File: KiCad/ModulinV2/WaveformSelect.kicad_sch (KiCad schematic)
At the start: 54 parts, among them IC10 TMUX4052DYYR, IC11 SN74AHCT1G00DBVR, IC12 SN74AHC1G02DBVR, IC13 TMUX4051DYYRQ1, IC14 TMUX4051DYYRQ1, IC15 SN74HC193DR, IC23 NC7SZ74K8X, IC24 SN74AHCT1G00DBVR, IC25 SN74AHC1G02DBVR, IC9 SN74AHCT1G00DBVR, J2 TSW-104-07-T-D, J6 TSW-104-07-T-D, J7 TSW-104-07-T-D, J8 TSW-104-07-T-D, U1 SN74AHC1G08DBVR

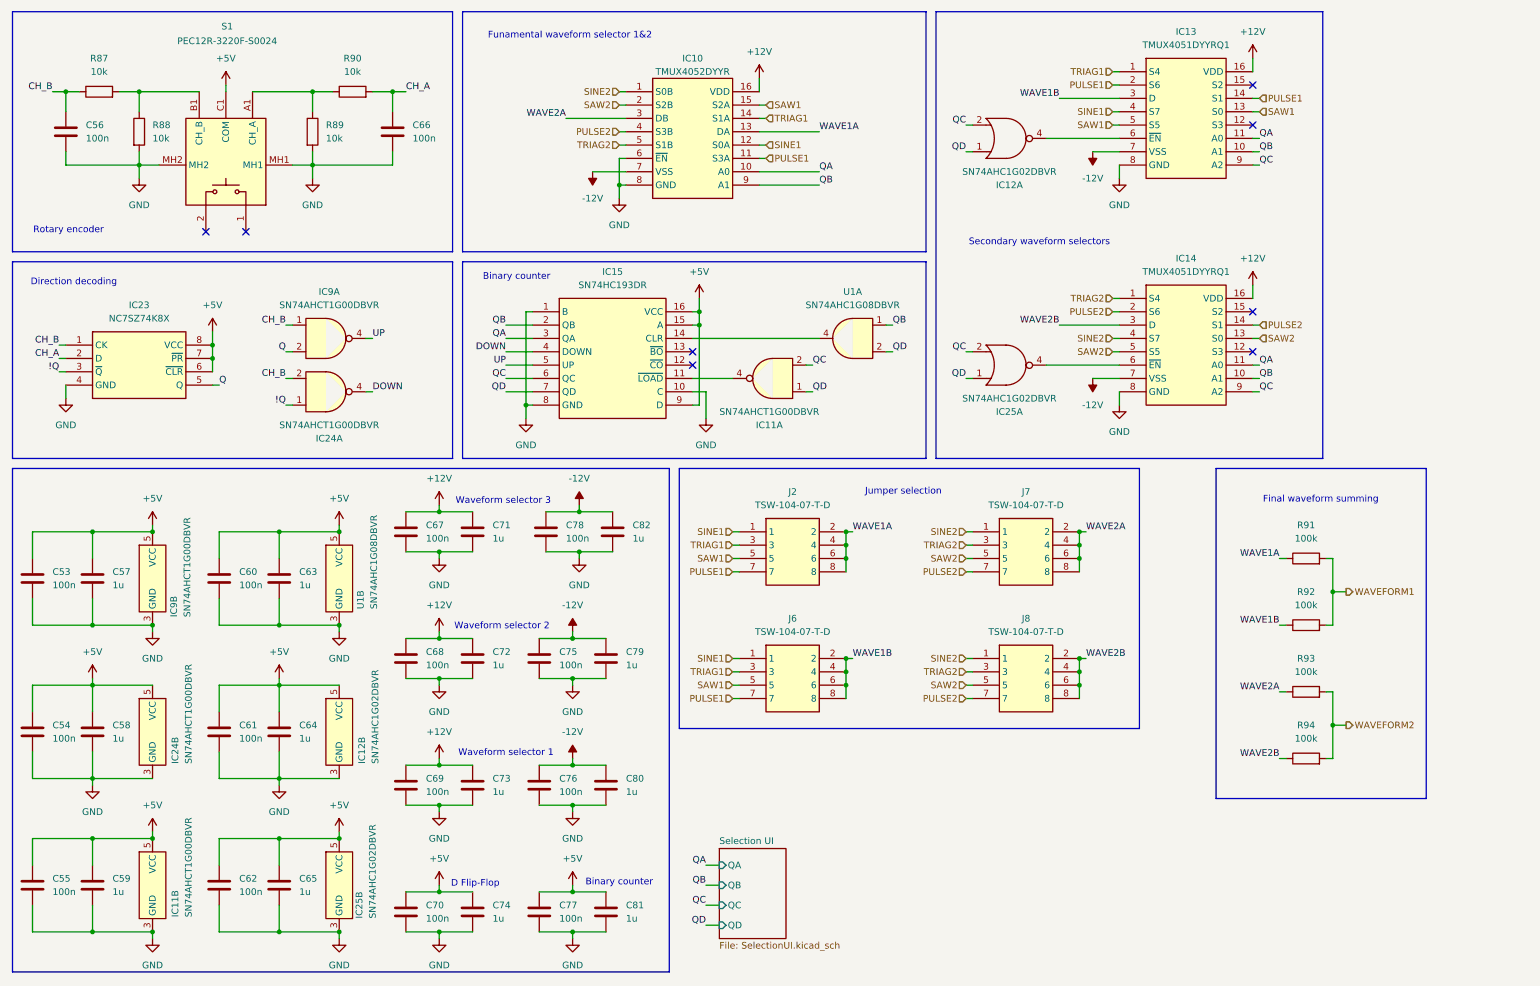
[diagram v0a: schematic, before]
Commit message: Changed switch for the boot and nrst. Fixed the GATE interface trigger
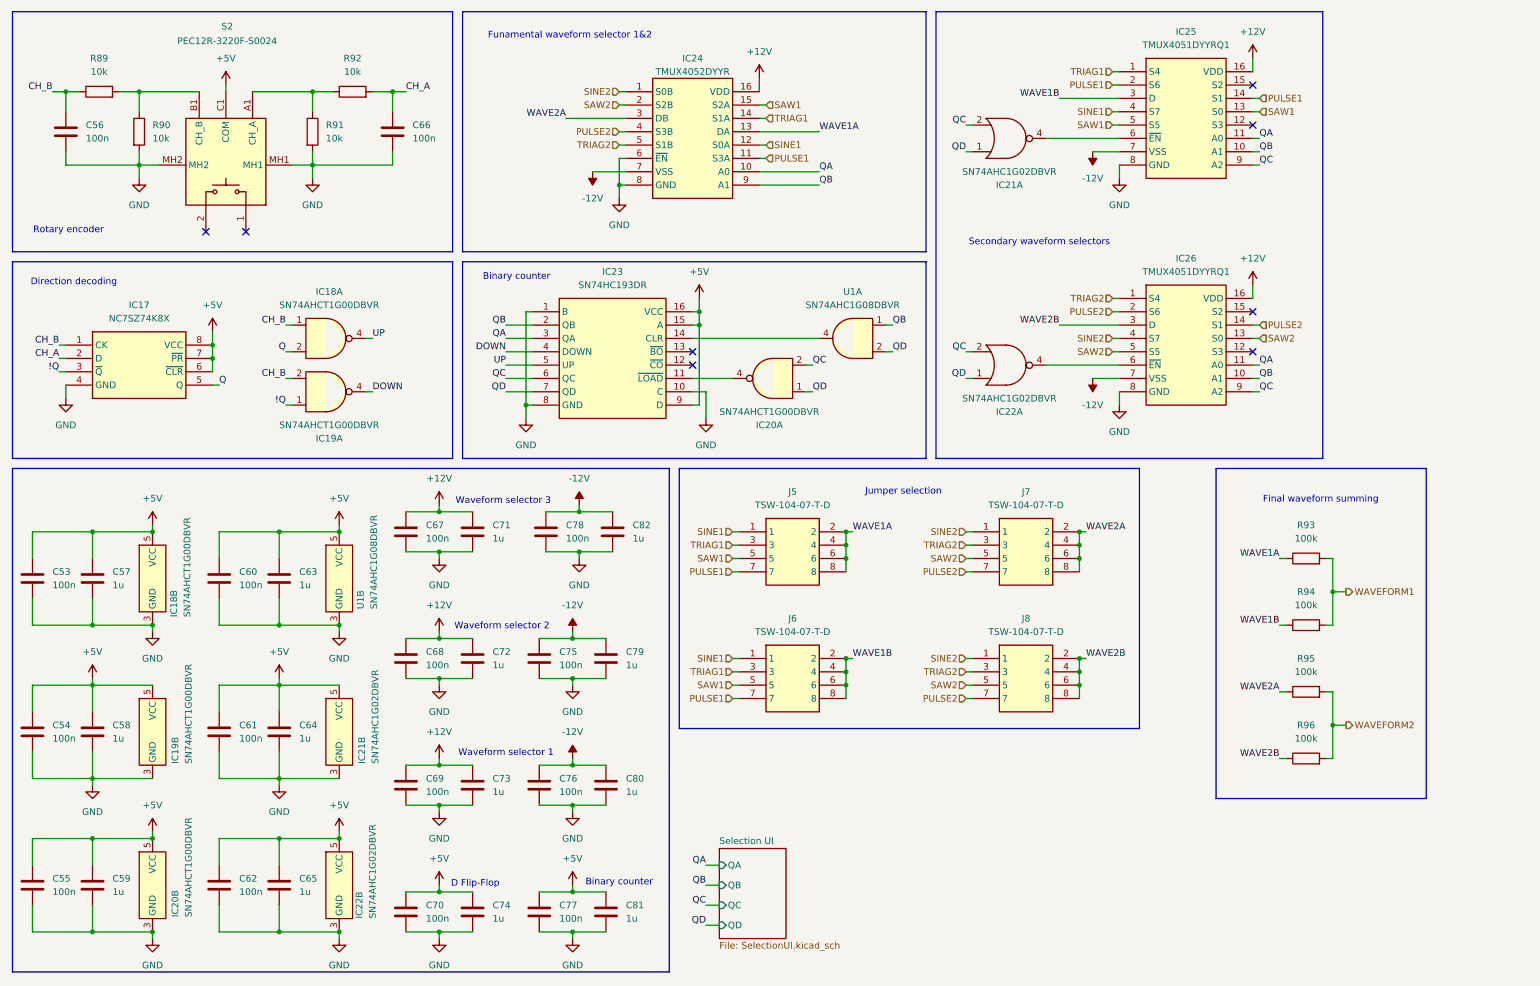
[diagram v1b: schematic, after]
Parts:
- renumbered IC23 to IC17, IC9 to IC18, IC24 to IC19, IC11 to IC20, IC12 to IC21, IC25 to IC22, IC15 to IC23, IC10 to IC24, IC13 to IC25, IC14 to IC26, J2 to J5, R87 to R89, R88 to R90, R89 to R91, R90 to R92, R91 to R93, R92 to R94, R93 to R95, R94 to R96, S1 to S2

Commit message: Started adding footprints for capacitors
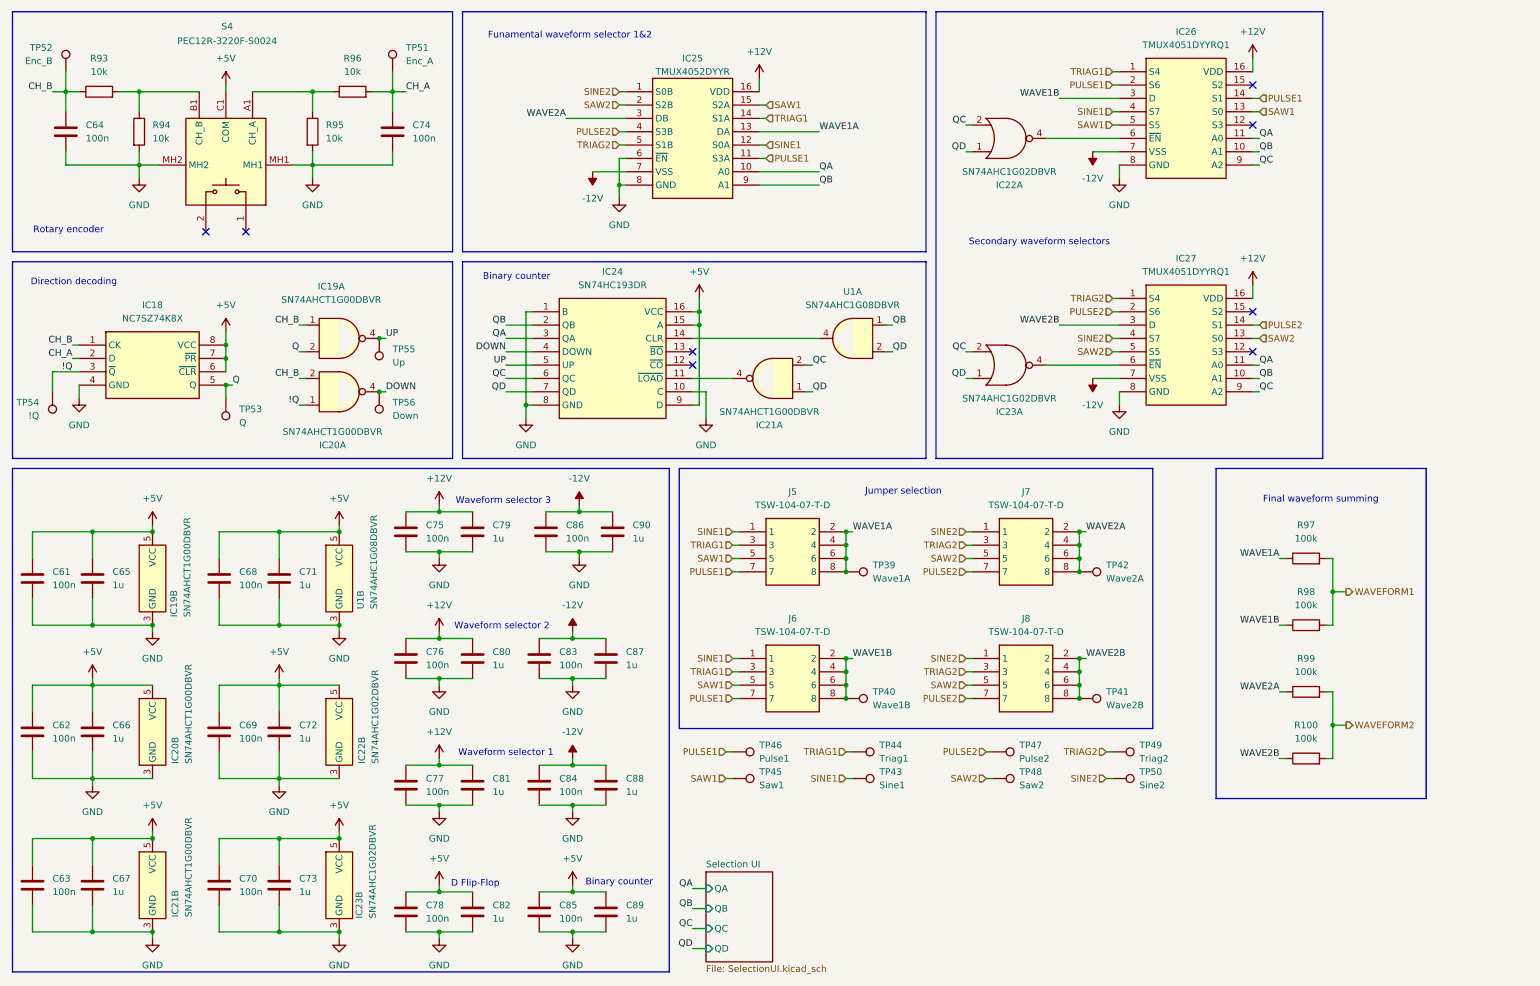
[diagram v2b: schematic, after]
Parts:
- added TP39: Wave1A, SamacSys_Parts:TestPointLoop, symbol Connector:TestPoint
- added TP40: Wave1B, SamacSys_Parts:TestPointLoop, symbol Connector:TestPoint
- added TP41: Wave2B, SamacSys_Parts:TestPointLoop, symbol Connector:TestPoint
- added TP42: Wave2A, SamacSys_Parts:TestPointLoop, symbol Connector:TestPoint
- added TP43: Sine1, SamacSys_Parts:TestPointLoop, symbol Connector:TestPoint
- added TP44: Triag1, SamacSys_Parts:TestPointLoop, symbol Connector:TestPoint
- added TP45: Saw1, SamacSys_Parts:TestPointLoop, symbol Connector:TestPoint
- added TP46: Pulse1, SamacSys_Parts:TestPointLoop, symbol Connector:TestPoint
- added TP47: Pulse2, SamacSys_Parts:TestPointLoop, symbol Connector:TestPoint
- added TP48: Saw2, SamacSys_Parts:TestPointLoop, symbol Connector:TestPoint
- added TP49: Triag2, SamacSys_Parts:TestPointLoop, symbol Connector:TestPoint
- added TP50: Sine2, SamacSys_Parts:TestPointLoop, symbol Connector:TestPoint
- added TP51: Enc_A, SamacSys_Parts:TestPointLoop, symbol Connector:TestPoint
- added TP52: Enc_B, SamacSys_Parts:TestPointLoop, symbol Connector:TestPoint
- added TP53: Q, SamacSys_Parts:TestPointLoop, symbol Connector:TestPoint
- added TP54: !Q, SamacSys_Parts:TestPointLoop, symbol Connector:TestPoint
- added TP55: Up, SamacSys_Parts:TestPointLoop, symbol Connector:TestPoint
- added TP56: Down, SamacSys_Parts:TestPointLoop, symbol Connector:TestPoint
- C61: renamed from C53; footprint (none) -> SamacSys_Parts:CAPC1608X90N
- C62: renamed from C54; footprint (none) -> SamacSys_Parts:CAPC1608X90N
- C63: renamed from C55; footprint (none) -> SamacSys_Parts:CAPC1608X90N
- C64: renamed from C56; footprint (none) -> SamacSys_Parts:CAPC1608X90N
- C65: renamed from C57; footprint (none) -> SamacSys_Parts:CAPC1608X95N
- C66: renamed from C58; footprint (none) -> SamacSys_Parts:CAPC1608X95N
- C67: renamed from C59; footprint (none) -> SamacSys_Parts:CAPC1608X95N
- C68: renamed from C60; footprint (none) -> SamacSys_Parts:CAPC1608X90N
- C69: renamed from C61; footprint (none) -> SamacSys_Parts:CAPC1608X90N
- C70: renamed from C62; footprint (none) -> SamacSys_Parts:CAPC1608X90N
- C71: renamed from C63; footprint (none) -> SamacSys_Parts:CAPC1608X95N
- C72: renamed from C64; footprint (none) -> SamacSys_Parts:CAPC1608X95N
- C73: renamed from C65; footprint (none) -> SamacSys_Parts:CAPC1608X95N
- C74: renamed from C66; footprint (none) -> SamacSys_Parts:CAPC1608X90N
- C75: renamed from C67; footprint (none) -> SamacSys_Parts:CAPC1608X90N
- C76: renamed from C68; footprint (none) -> SamacSys_Parts:CAPC1608X90N
- C77: renamed from C69; footprint (none) -> SamacSys_Parts:CAPC1608X90N
- C78: renamed from C70; footprint (none) -> SamacSys_Parts:CAPC1608X90N
- C79: renamed from C71; footprint (none) -> SamacSys_Parts:CAPC1608X95N
- C80: renamed from C72; footprint (none) -> SamacSys_Parts:CAPC1608X95N
- C81: renamed from C73; footprint (none) -> SamacSys_Parts:CAPC1608X95N
- C82: renamed from C74; footprint (none) -> SamacSys_Parts:CAPC1608X95N
- C83: renamed from C75; footprint (none) -> SamacSys_Parts:CAPC1608X90N
- C84: renamed from C76; footprint (none) -> SamacSys_Parts:CAPC1608X90N
- C85: renamed from C77; footprint (none) -> SamacSys_Parts:CAPC1608X90N
- C86: renamed from C78; footprint (none) -> SamacSys_Parts:CAPC1608X90N
- C87: renamed from C79; footprint (none) -> SamacSys_Parts:CAPC1608X95N
- C88: renamed from C80; footprint (none) -> SamacSys_Parts:CAPC1608X95N
- C89: renamed from C81; footprint (none) -> SamacSys_Parts:CAPC1608X95N
- C90: renamed from C82; footprint (none) -> SamacSys_Parts:CAPC1608X95N
- renumbered IC17 to IC18, IC18 to IC19, IC19 to IC20, IC20 to IC21, IC21 to IC22, IC22 to IC23, IC23 to IC24, IC24 to IC25, IC25 to IC26, IC26 to IC27, R96 to R100, R89 to R93, R90 to R94, R91 to R95, R92 to R96, R93 to R97, R94 to R98, R95 to R99, S2 to S4
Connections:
- net !Q: now also TP54.1
- net CH_A: now also TP51.1
- net CH_B: now also TP52.1
- net DOWN: now also TP56.1
- net PULSE1: now also TP46.1
- net PULSE2: now also TP47.1
- net Q: now also TP53.1
- net SAW1: now also TP45.1
- net SAW2: now also TP48.1
- net SINE1: now also TP43.1
- net SINE2: now also TP50.1
- net TRIAG1: now also TP44.1
- net TRIAG2: now also TP49.1
- net UP: now also TP55.1
- net WAVE1A: now also TP39.1
- net WAVE1B: now also TP40.1
- net WAVE2A: now also TP42.1
- net WAVE2B: now also TP41.1
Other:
- moved on the sheet: IC18, IC19A, IC20A

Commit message: Added footprints to all capacitors and potentiometers
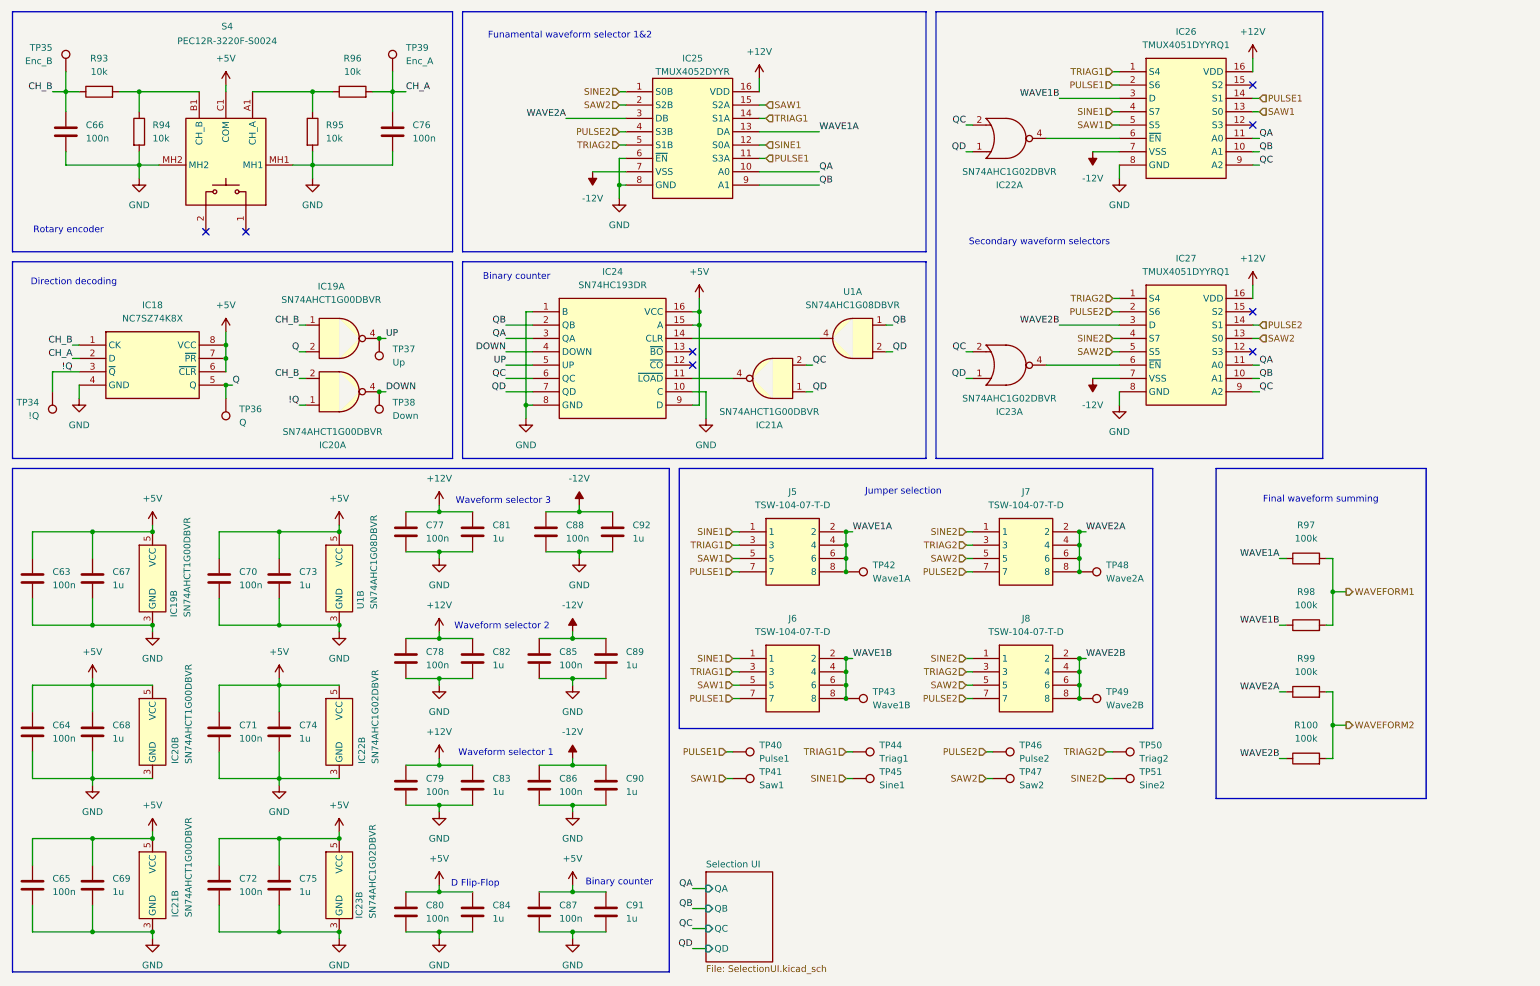
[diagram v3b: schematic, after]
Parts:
- C63: renamed from C61; footprint SamacSys_Parts:CAPC1608X90N -> Capacitor_SMD:C_0603_1608Metric_Pad1.08x0.95mm_HandSolder
- C64: renamed from C62; footprint SamacSys_Parts:CAPC1608X90N -> Capacitor_SMD:C_0603_1608Metric_Pad1.08x0.95mm_HandSolder
- C65: renamed from C63; footprint SamacSys_Parts:CAPC1608X90N -> Capacitor_SMD:C_0603_1608Metric_Pad1.08x0.95mm_HandSolder
- C66: renamed from C64; footprint SamacSys_Parts:CAPC1608X90N -> Capacitor_SMD:C_0603_1608Metric_Pad1.08x0.95mm_HandSolder
- C67: renamed from C65; footprint SamacSys_Parts:CAPC1608X95N -> Capacitor_SMD:C_0603_1608Metric_Pad1.08x0.95mm_HandSolder
- C68: renamed from C66; footprint SamacSys_Parts:CAPC1608X95N -> Capacitor_SMD:C_0603_1608Metric_Pad1.08x0.95mm_HandSolder
- C69: renamed from C67; footprint SamacSys_Parts:CAPC1608X95N -> Capacitor_SMD:C_0603_1608Metric_Pad1.08x0.95mm_HandSolder
- C70: renamed from C68; footprint SamacSys_Parts:CAPC1608X90N -> Capacitor_SMD:C_0603_1608Metric_Pad1.08x0.95mm_HandSolder
- C71: renamed from C69; footprint SamacSys_Parts:CAPC1608X90N -> Capacitor_SMD:C_0603_1608Metric_Pad1.08x0.95mm_HandSolder
- C72: renamed from C70; footprint SamacSys_Parts:CAPC1608X90N -> Capacitor_SMD:C_0603_1608Metric_Pad1.08x0.95mm_HandSolder
- C73: renamed from C71; footprint SamacSys_Parts:CAPC1608X95N -> Capacitor_SMD:C_0603_1608Metric_Pad1.08x0.95mm_HandSolder
- C74: renamed from C72; footprint SamacSys_Parts:CAPC1608X95N -> Capacitor_SMD:C_0603_1608Metric_Pad1.08x0.95mm_HandSolder
- C75: renamed from C73; footprint SamacSys_Parts:CAPC1608X95N -> Capacitor_SMD:C_0603_1608Metric_Pad1.08x0.95mm_HandSolder
- C76: renamed from C74; footprint SamacSys_Parts:CAPC1608X90N -> Capacitor_SMD:C_0603_1608Metric_Pad1.08x0.95mm_HandSolder
- C77: renamed from C75; footprint SamacSys_Parts:CAPC1608X90N -> Capacitor_SMD:C_0603_1608Metric_Pad1.08x0.95mm_HandSolder
- C78: renamed from C76; footprint SamacSys_Parts:CAPC1608X90N -> Capacitor_SMD:C_0603_1608Metric_Pad1.08x0.95mm_HandSolder
- C79: renamed from C77; footprint SamacSys_Parts:CAPC1608X90N -> Capacitor_SMD:C_0603_1608Metric_Pad1.08x0.95mm_HandSolder
- C80: renamed from C78; footprint SamacSys_Parts:CAPC1608X90N -> Capacitor_SMD:C_0603_1608Metric_Pad1.08x0.95mm_HandSolder
- C81: renamed from C79; footprint SamacSys_Parts:CAPC1608X95N -> Capacitor_SMD:C_0603_1608Metric_Pad1.08x0.95mm_HandSolder
- C82: renamed from C80; footprint SamacSys_Parts:CAPC1608X95N -> Capacitor_SMD:C_0603_1608Metric_Pad1.08x0.95mm_HandSolder
- C83: renamed from C81; footprint SamacSys_Parts:CAPC1608X95N -> Capacitor_SMD:C_0603_1608Metric_Pad1.08x0.95mm_HandSolder
- C84: renamed from C82; footprint SamacSys_Parts:CAPC1608X95N -> Capacitor_SMD:C_0603_1608Metric_Pad1.08x0.95mm_HandSolder
- C85: renamed from C83; footprint SamacSys_Parts:CAPC1608X90N -> Capacitor_SMD:C_0603_1608Metric_Pad1.08x0.95mm_HandSolder
- C86: renamed from C84; footprint SamacSys_Parts:CAPC1608X90N -> Capacitor_SMD:C_0603_1608Metric_Pad1.08x0.95mm_HandSolder
- C87: renamed from C85; footprint SamacSys_Parts:CAPC1608X90N -> Capacitor_SMD:C_0603_1608Metric_Pad1.08x0.95mm_HandSolder
- C88: renamed from C86; footprint SamacSys_Parts:CAPC1608X90N -> Capacitor_SMD:C_0603_1608Metric_Pad1.08x0.95mm_HandSolder
- C89: renamed from C87; footprint SamacSys_Parts:CAPC1608X95N -> Capacitor_SMD:C_0603_1608Metric_Pad1.08x0.95mm_HandSolder
- C90: renamed from C88; footprint SamacSys_Parts:CAPC1608X95N -> Capacitor_SMD:C_0603_1608Metric_Pad1.08x0.95mm_HandSolder
- C91: renamed from C89; footprint SamacSys_Parts:CAPC1608X95N -> Capacitor_SMD:C_0603_1608Metric_Pad1.08x0.95mm_HandSolder
- C92: renamed from C90; footprint SamacSys_Parts:CAPC1608X95N -> Capacitor_SMD:C_0603_1608Metric_Pad1.08x0.95mm_HandSolder
- renumbered TP54 to TP34, TP52 to TP35, TP53 to TP36, TP55 to TP37, TP56 to TP38, TP51 to TP39, TP46 to TP40, TP45 to TP41, TP39 to TP42, TP40 to TP43, TP43 to TP45, TP47 to TP46, TP48 to TP47, TP42 to TP48, TP41 to TP49, TP49 to TP50, TP50 to TP51
